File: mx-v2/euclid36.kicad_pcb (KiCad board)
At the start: 2 copper layers, 248.2 x 127 mm, 123 parts, among them SW1 RotaryEncoder_Switch, SW10 SW_PUSH, SW11 SW_PUSH, SW12 SW_PUSH, SW14 SW_PUSH, SW15 SW_PUSH, SW16 SW_PUSH, SW17 SW_PUSH, SW18 SW_PUSH, SW19 SW_PUSH, SW2 SW_PUSH, SW20 SW_PUSH, SW21 SW_PUSH, SW22 SW_PUSH, SW23 SW_PUSH, SW25 SW_PUSH, SW26 SW_PUSH, SW27 SW_PUSH, SW28 SW_PUSH, SW29 SW_PUSH, SW3 SW_PUSH, SW31 SW_PUSH, SW32 SW_PUSH, SW33 SW_PUSH, SW34 SW_PUSH, SW35 SW_PUSH, SW37 SW_PUSH, SW38 SW_PUSH, SW39 SW_PUSH, SW4 SW_PUSH, SW40 SW_PUSH, SW41 SW_PUSH, SW42 SW_PUSH, SW5 SW_PUSH, SW6 SW_PUSH, SW7 RotaryEncoder_Switch, SW8 SW_PUSH, SW9 SW_PUSH, U1 USBLC6-2SC6, U2 ATmega32U4-AU, Y1 XTAL

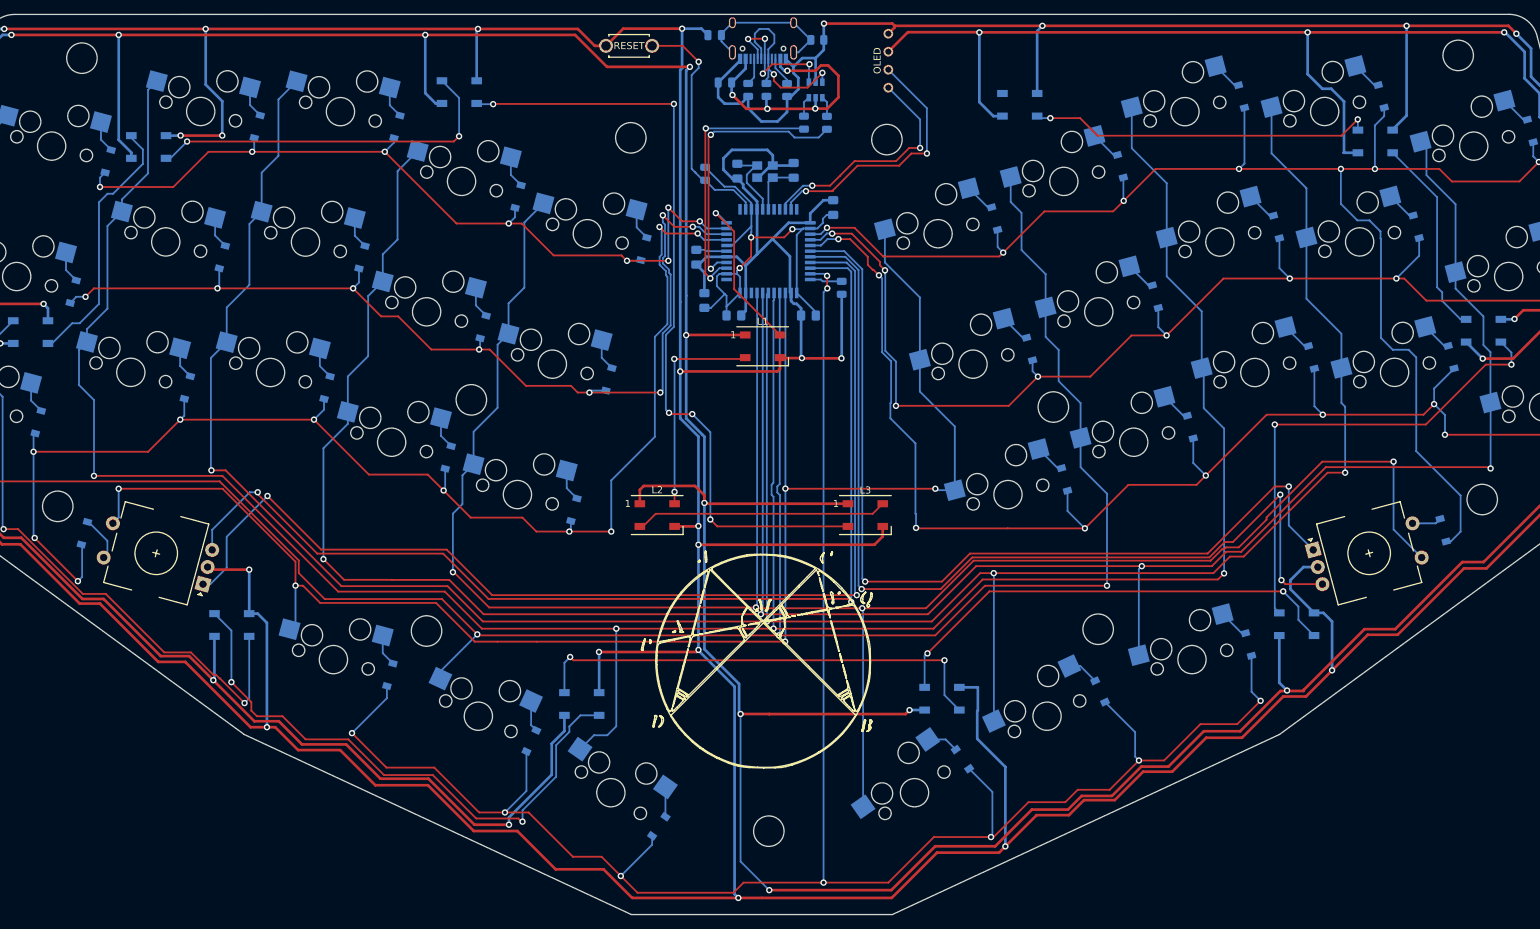
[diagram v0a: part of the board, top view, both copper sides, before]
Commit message: Added support for two joysticks, but can't use both at the same time, as they share pins
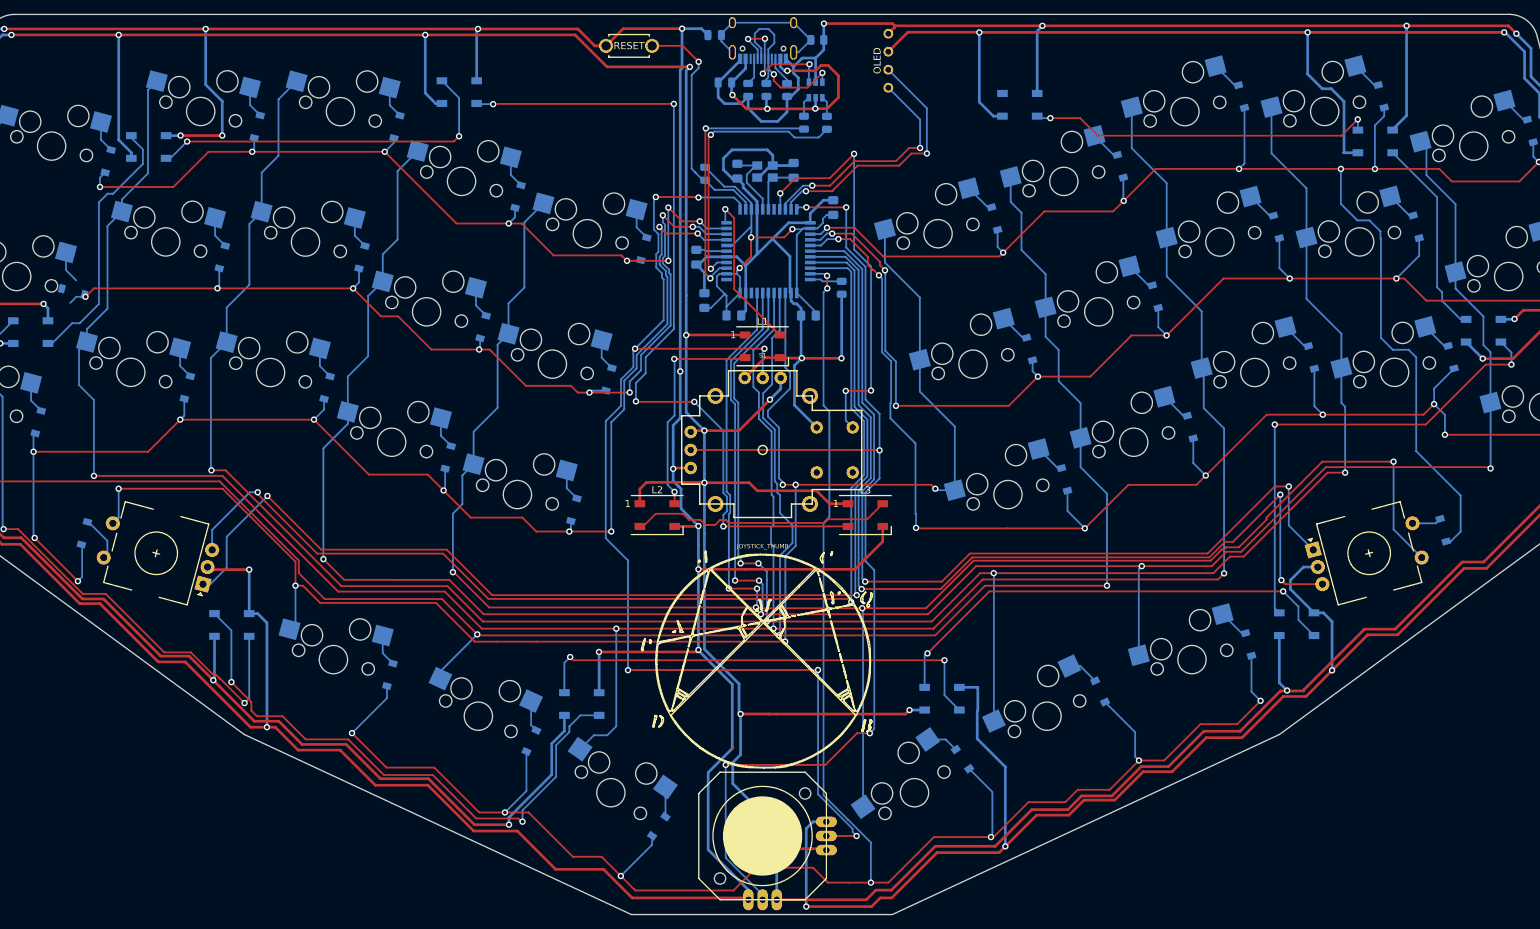
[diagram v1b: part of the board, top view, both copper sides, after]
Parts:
- removed Ref** (x11): Val**, _reviung-kbd:spacer_m2
- added JOY1: JOYSTICK_ANALOG_XY, adafruit-analog-thumbstick:JOYSTICK_ANALOG_MINITHM, F.Cu at (150.6, 141.3)
- added S1: JOYSTICK_THUMB, SparkFun-Switches:JOYSTICK, F.Cu at (150.6, 86.9)
- turned D8 to 165 degrees
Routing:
- net Net-(JOY1-PadX): track 0.00 -> 164.7 mm, vias 0 -> 7
- net Net-(JOY1-PadY): track 0.00 -> 154.9 mm, vias 0 -> 5
- net Net-(S1-PadB1A): track 0.00 -> 58.6 mm, vias 0 -> 4
- net VCC: track 891.7 -> 918.6 mm, vias 21 -> 23
- net GND: track 1137.8 -> 1155.4 mm, vias 28 -> 29
- net Net-(L3-Pad2): track 111.2 -> 117.6 mm
- net col5: track 288.6 -> 294.6 mm, vias 4 -> 6
- net col4: track 348.0 -> 353.7 mm, vias 4 -> 6
- net col3: track 360.6 -> 366.2 mm, vias 4 -> 6
- net row6: track 291.3 -> 296.2 mm
- net col0: track 230.7 -> 234.4 mm, vias 5 -> 6
- net col2: track 371.7 -> 375.3 mm
- net col1: track 352.5 -> 355.6 mm
- net row1: track 136.8 -> 134.2 mm
- net ENC1A: track 158.4 -> 160.2 mm
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
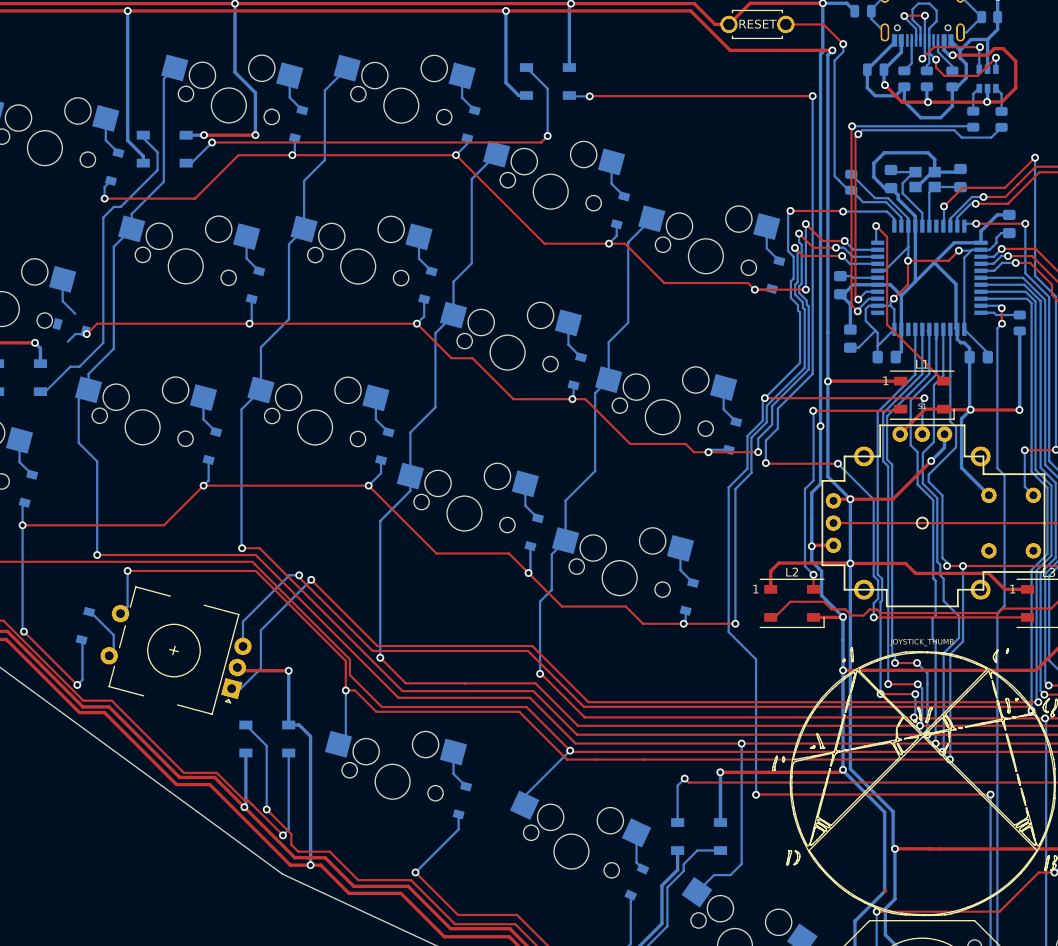
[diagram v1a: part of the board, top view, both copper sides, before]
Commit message: whoops, ran drc and had to fix a few things
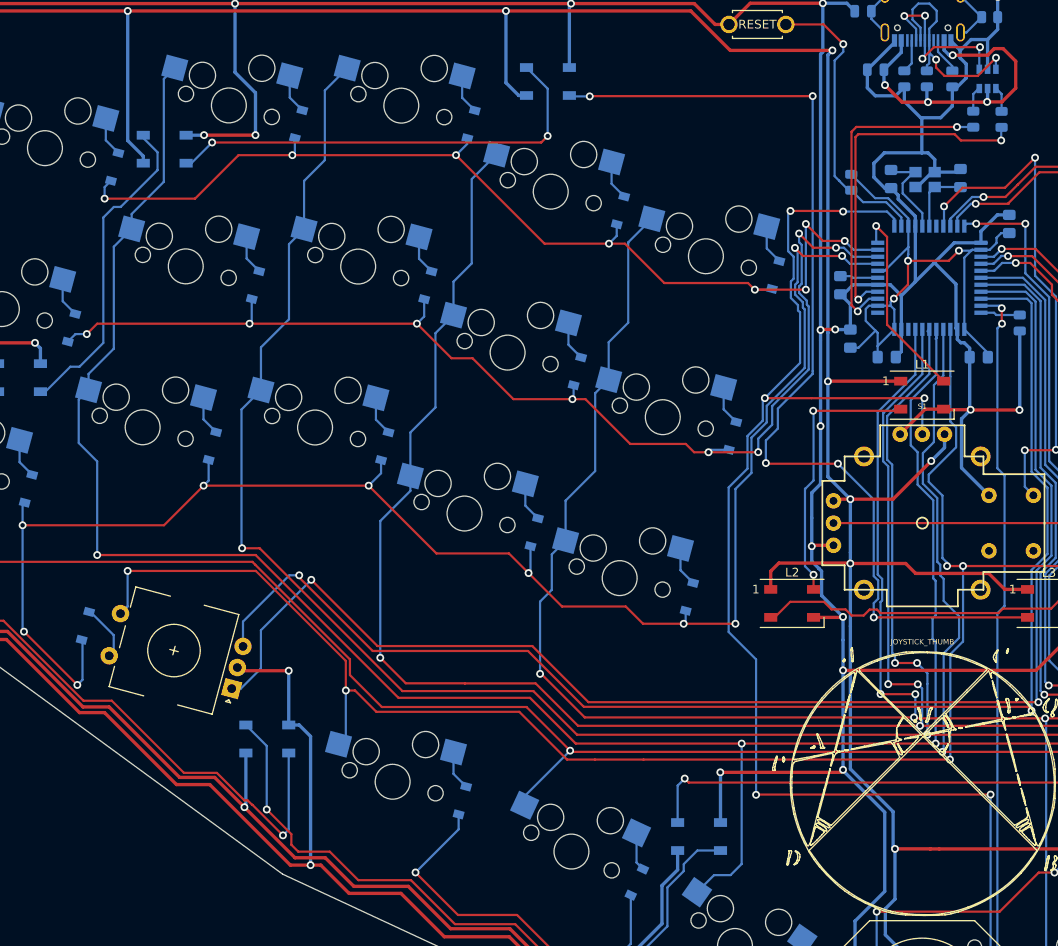
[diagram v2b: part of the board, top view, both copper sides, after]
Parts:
- turned D8 to 75 degrees
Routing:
- net GND: track 1155.4 -> 1162.7 mm, vias 29 -> 31
- net D+: track 39.2 -> 39.9 mm
- net (no net): track 0.51 -> 0.00 mm
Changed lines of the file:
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@@
     (thickness 1.6)
     (drawings 2733)
-    (tracks 1794)
+    (tracks 1806)
     (zones 0)
     (modules 114)
@@
   )
   (module Diode_SMD:D_SOD-123 (layer B.Cu)
-    (at 53.340669 64.525068 165)
+    (at 53.340669 64.525068 75)
     (descr SOD-123)
     (tags SOD-123)
     (attr smd)
-    (fp_text reference D8 (at 0 2 345) (layer B.SilkS)
+    (fp_text reference D8 (at 0 2 255) (layer B.SilkS)
       (effects (font (size 1 1) (thickness 0.15)) (justify mirror))
     )
-    (fp_text value 1N4148W (at 0 -2.1 345) (layer B.Fab)
+    (fp_text value 1N4148W (at 0 -2.1 255) (layer B.Fab)
       (effects (font (size 1 1) (thickness 0.15)) (justify mirror))
     )
@@
     (fp_line (start -2.25 -1) (end 1.65 -1) (layer B.SilkS) (width 0.12))
     (fp_line (start -2.25 1) (end 1.65 1) (layer B.SilkS) (width 0.12))
-    (fp_text user %R (at 0 2 345) (layer B.Fab)
+    (fp_text user %R (at 0 2 255) (layer B.Fab)
       (effects (font (size 1 1) (thickness 0.15)) (justify mirror))
     )
-    (pad 1 smd rect (at -1.65 0 165) (size 0.9 1.2) (layers B.Cu B.Paste B.Mask)
+    (pad 1 smd rect (at -1.65 0 75) (size 0.9 1.2) (layers B.Cu B.Paste B.Mask)
       (net 7 row1))
-    (pad 2 smd rect (at 1.65 0 165) (size 0.9 1.2) (layers B.Cu B.Paste B.Mask)
+    (pad 2 smd rect (at 1.65 0 75) (size 0.9 1.2) (layers B.Cu B.Paste B.Mask)
       (net 8 "Net-(D8-Pad2)"))
     (model ${KISYS3DMOD}/Diode_SMD.3dshapes/D_SOD-123.wrl
@@
   (segment (start 147.4905 124.11) (end 151.53 124.11) (width 0.381) (layer F.Cu) (net 44))
   (segment (start 142.390501 98.649499) (end 142.390501 114.970501) (width 0.381) (layer B.Cu) (net 44))
-  (segment (start 144.17 93.82) (end 144.53 94.18) (width 0.381) (layer B.Cu) (net 0))
   (segment (start 132.475 148.845) (end 130.595 146.965) (width 0.254) (layer F.Cu) (net 37))
   (segment (start 132.64 149.01) (end 132.475 148.845) (width 0.254) (layer F.Cu) (net 37))
@@
   (segment (start 139.24 32.98) (end 138.98051 33.23949) (width 0.381) (layer B.Cu) (net 45))
   (segment (start 138.98051 65.95949) (end 138.98051 75.78) (width 0.381) (layer B.Cu) (net 45))
-  (segment (start 138.98051 33.23949) (end 138.98051 65.95949) (width 0.381) (layer B.Cu) (net 45))
   (via (at 78.17 103.74) (size 0.9) (drill 0.5) (layers F.Cu B.Cu) (net 45))
   (segment (start 78.17 109.95) (end 78.17 103.74) (width 0.381) (layer B.Cu) (net 45))
@@
   (segment (start 148.56 36.9725) (end 148.56 38.64) (width 0.381) (layer B.Cu) (net 45))
   (segment (start 148.56 38.64) (end 150.43 40.51) (width 0.381) (layer B.Cu) (net 45))
-  (segment (start 150.43 40.51) (end 152.72 40.51) (width 0.381) (layer B.Cu) (net 45))
   (segment (start 154.05 39.18) (end 154.05 36.9825) (width 0.381) (layer B.Cu) (net 45))
   (segment (start 152.72 40.51) (end 154.05 39.18) (width 0.381) (layer B.Cu) (net 45))
@@
   (segment (start 145.08 47.32) (end 145.08 45.72) (width 0.381) (layer B.Cu) (net 45))
   (segment (start 145.08 45.72) (end 146.28 44.52) (width 0.381) (layer B.Cu) (net 45))
-  (segment (start 146.28 44.52) (end 151.27 44.52) (width 0.381) (layer B.Cu) (net 45))
   (segment (start 152.04 45.29) (end 152.04 46.73) (width 0.381) (layer B.Cu) (net 45))
   (segment (start 151.27 44.52) (end 152.04 45.29) (width 0.381) (layer B.Cu) (net 45))
@@
   (segment (start 137.977 89.517) (end 137.977 91.237) (width 0.381) (layer B.Cu) (net 45))
   (segment (start 137.977 86.27) (end 137.977 89.517) (width 0.381) (layer B.Cu) (net 45))
-  (segment (start 146.43 128.86) (end 146.32 128.97) (width 0.381) (layer F.Cu) (net 45))
   (segment (start 148.34 150.06) (end 148.6 150.32) (width 0.381) (layer F.Cu) (net 45))
   (segment (start 132.2 150.06) (end 148.34 150.06) (width 0.381) (layer F.Cu) (net 45))
@@
   (segment (start 156.76 140.279) (end 157.719 139.32) (width 0.381) (layer B.Cu) (net 45))
   (segment (start 156.76 151.28) (end 156.76 140.279) (width 0.381) (layer B.Cu) (net 45))
+  (via (at 140.66151 64.72) (size 0.9) (drill 0.5) (layers F.Cu B.Cu) (net 45))
+  (segment (start 140.67401 64.7325) (end 140.66151 64.72) (width 0.381) (layer B.Cu) (net 45))
+  (segment (start 142.39 64.7325) (end 140.67401 64.7325) (width 0.381) (layer B.Cu) (net 45))
+  (via (at 138.98051 64.77949) (size 0.9) (drill 0.5) (layers F.Cu B.Cu) (net 45))
+  (segment (start 139.04 64.72) (end 138.98051 64.77949) (width 0.381) (layer F.Cu) (net 45))
+  (segment (start 140.66151 64.72) (end 139.04 64.72) (width 0.381) (layer F.Cu) (net 45))
+  (segment (start 138.98051 64.77949) (end 138.98051 65.95949) (width 0.381) (layer B.Cu) (net 45))
+  (segment (start 138.98051 33.23949) (end 138.98051 64.77949) (width 0.381) (layer B.Cu) (net 45))
+  (segment (start 150.56 40.54) (end 150.53 40.51) (width 0.381) (layer B.Cu) (net 45))
+  (segment (start 150.56 44.52) (end 150.56 40.54) (width 0.381) (layer B.Cu) (net 45))
+  (segment (start 150.43 40.51) (end 150.53 40.51) (width 0.381) (layer B.Cu) (net 45))
+  (segment (start 150.53 40.51) (end 152.72 40.51) (width 0.381) (layer B.Cu) (net 45))
+  (segment (start 146.28 44.52) (end 150.56 44.52) (width 0.381) (layer B.Cu) (net 45))
+  (segment (start 150.56 44.52) (end 151.27 44.52) (width 0.381) (layer B.Cu) (net 45))
   (via (at 153.78 113.9) (size 0.9) (drill 0.5) (layers F.Cu B.Cu) (net 46))
   (segment (start 153.78 113.9) (end 118.74 113.9) (width 0.254) (layer F.Cu) (net 46))
@@
   (segment (start 144.516 61.21) (end 143.2305 62.4955) (width 0.254) (layer B.Cu) (net 83))
   (segment (start 145.52 61.21) (end 144.516 61.21) (width 0.254) (layer B.Cu) (net 83))
-  (segment (start 143.2305 62.648093) (end 142.52 61.937593) (width 0.254) (layer F.Cu) (net 83))
-  (via (at 142.59 41.49) (size 0.9) (drill 0.5) (layers F.Cu B.Cu) (net 83))
-  (segment (start 142.52 41.56) (end 142.59 41.49) (width 0.254) (layer F.Cu) (net 83))
-  (segment (start 142.52 61.937593) (end 142.52 41.56) (width 0.254) (layer F.Cu) (net 83))
   (segment (start 156.3375 41.49) (end 156.44 41.5925) (width 0.254) (layer B.Cu) (net 83))
-  (segment (start 142.59 41.49) (end 156.3375 41.49) (width 0.254) (layer B.Cu) (net 83))
+  (via (at 154.58 41.57) (size 0.9) (drill 0.5) (layers F.Cu B.Cu) (net 83))
+  (segment (start 156.4175 41.57) (end 156.44 41.5925) (width 0.254) (layer B.Cu) (net 83))
+  (segment (start 154.58 41.57) (end 156.4175 41.57) (width 0.254) (layer B.Cu) (net 83))
+  (segment (start 142.52 61.937593) (end 143.2305 62.648093) (width 0.254) (layer F.Cu) (net 83))
+  (segment (start 142.52 42.12) (end 142.52 61.937593) (width 0.254) (layer F.Cu) (net 83))
+  (segment (start 143.08 41.56) (end 142.52 42.12) (width 0.254) (layer F.Cu) (net 83))
+  (segment (start 154.57 41.56) (end 143.08 41.56) (width 0.254) (layer F.Cu) (net 83))
+  (segment (start 154.58 41.57) (end 154.57 41.56) (width 0.254) (layer F.Cu) (net 83))
   (segment (start 159.03 37.17) (end 159.06 37.17) (width 0.254) (layer B.Cu) (net 84))
   (segment (start 159.68 37.79) (end 159.68 39.7875) (width 0.254) (layer B.Cu) (net 84))
@@
   (segment (start 143.297 61.3) (end 142.97401 60.97701) (width 0.254) (layer F.Cu) (net 85))
   (segment (start 142.97401 42.715261) (end 143.297 42.392271) (width 0.254) (layer F.Cu) (net 85))
-  (via (at 143.297 42.392271) (size 0.9) (drill 0.5) (layers F.Cu B.Cu) (net 85))
   (segment (start 142.97401 60.97701) (end 142.97401 42.715261) (width 0.254) (layer F.Cu) (net 85))
-  (segment (start 143.297 42.392271) (end 143.745261 41.94401) (width 0.254) (layer B.Cu) (net 85))
-  (segment (start 143.745261 41.94401) (end 154.28401 41.94401) (width 0.254) (layer B.Cu) (net 85))
-  (segment (start 154.28401 41.94401) (end 155.12 42.78) (width 0.254) (layer B.Cu) (net 85))
-  (segment (start 158.5125 42.78) (end 159.68 41.6125) (width 0.254) (layer B.Cu) (net 85))
-  (segment (start 155.12 42.78) (end 158.5125 42.78) (width 0.254) (layer B.Cu) (net 85))
+  (segment (start 143.297 42.392271) (end 154.312271 42.392271) (width 0.254) (layer F.Cu) (net 85))
+  (via (at 159.64 43.11) (size 0.9) (drill 0.5) (layers F.Cu B.Cu) (net 85))
+  (segment (start 155.03 43.11) (end 159.64 43.11) (width 0.254) (layer F.Cu) (net 85))
+  (segment (start 154.312271 42.392271) (end 155.03 43.11) (width 0.254) (layer F.Cu) (net 85))
+  (segment (start 159.64 41.6525) (end 159.68 41.6125) (width 0.254) (layer B.Cu) (net 85))
+  (segment (start 159.64 43.11) (end 159.64 41.6525) (width 0.254) (layer B.Cu) (net 85))
   (segment (start 149.41 34.2975) (end 149.41 31.675) (width 0.254) (layer B.Cu) (net 86))
   (segment (start 148.56 35.1475) (end 149.41 34.2975) (width 0.254) (layer B.Cu) (net 86))
